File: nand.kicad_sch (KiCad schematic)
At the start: 4 parts, among them Q557 DMP3099L, Q558 2N7002, Q559 2N7002, Q560 DMP3099L

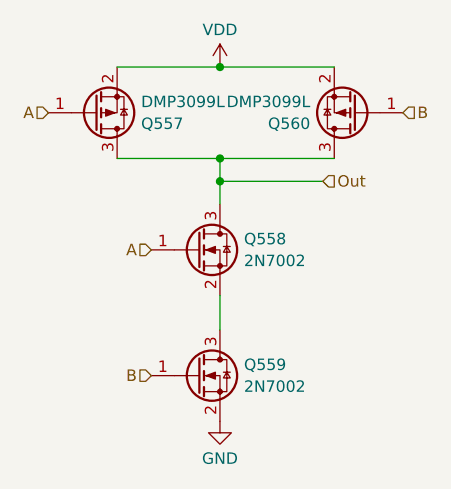
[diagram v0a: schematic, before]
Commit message: added decoupling caps
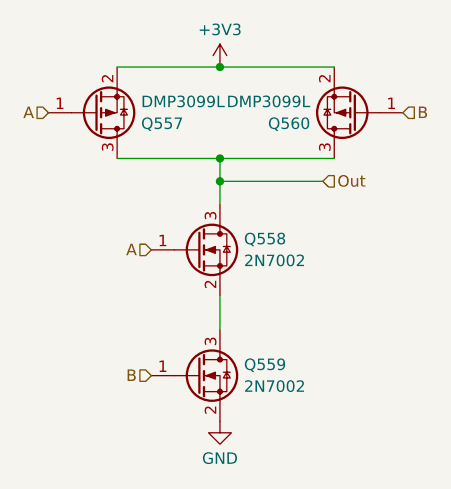
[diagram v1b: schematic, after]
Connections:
- net VDD renamed +3V3
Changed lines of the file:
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@@
+	(wire
+		(pts
+			(xy 115.57 74.93) (xy 128.27 74.93)
+		)
+		(stroke
+			(width 0)
+			(type default)
+		)
+	)
 	(wire
 		(pts
@@
 		(pts
 			(xy 104.14 85.09) (xy 115.57 85.09)
-		)
-		(stroke
-			(width 0)
-			(type default)
-		)
-	)
-	(wire
-		(pts
-			(xy 115.57 74.93) (xy 128.27 74.93)
 		)
 		(stroke
@@
 	)
 	(symbol
-		(lib_id "power:VDD")
+		(lib_id "power:+3V3")
 		(at 115.57 74.93 0)
 		(unit 1)
@@
 			)
 		)
-		(property "Value" "VDD"
+		(property "Value" "+3V3"
 			(at 115.57 70.7969 0)
 			(effects
@@
 			)
 		)
-		(property "Description" "Power symbol creates a global label with name \"VDD\""
+		(property "Description" "Power symbol creates a global label with name \"+3V3\""
 			(at 115.57 74.93 0)
 			(effects

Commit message: corrected output/input type of pins
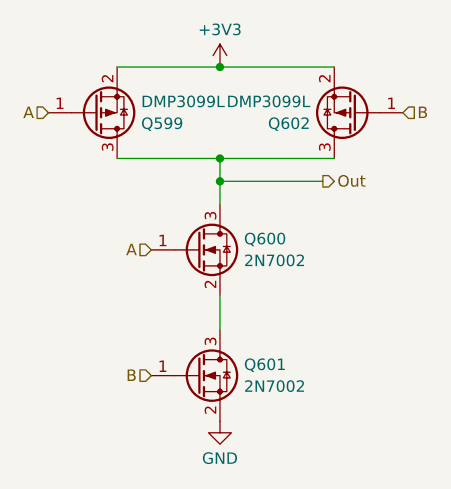
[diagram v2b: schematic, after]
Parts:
- renumbered Q557 to Q599, Q558 to Q600, Q559 to Q601, Q560 to Q602

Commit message: schematic cleanup, routed 1 bdc
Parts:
- renumbered Q599 to Q835, Q600 to Q836, Q601 to Q837, Q602 to Q838

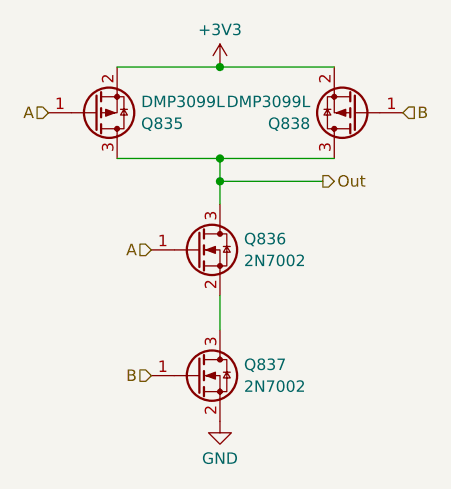
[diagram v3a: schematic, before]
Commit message: started on binary to decimal converter
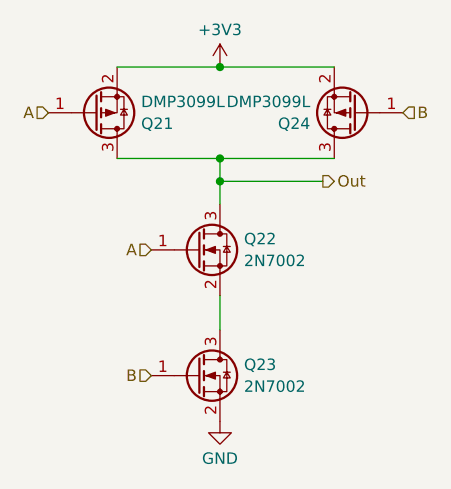
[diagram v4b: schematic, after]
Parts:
- renumbered Q835 to Q21, Q836 to Q22, Q837 to Q23, Q838 to Q24

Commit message: replace bcd logic with bin-to-dec module
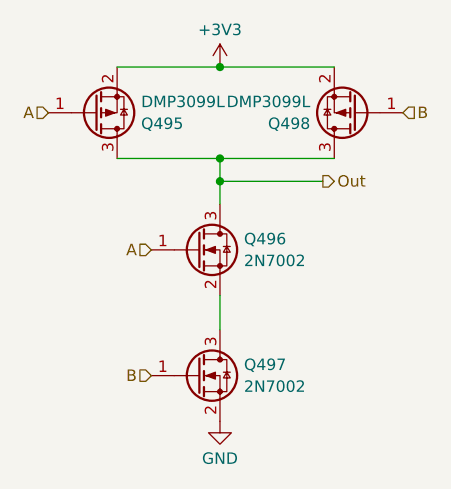
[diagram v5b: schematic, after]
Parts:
- renumbered Q21 to Q495, Q22 to Q496, Q23 to Q497, Q24 to Q498

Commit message: switched to using flipflop module
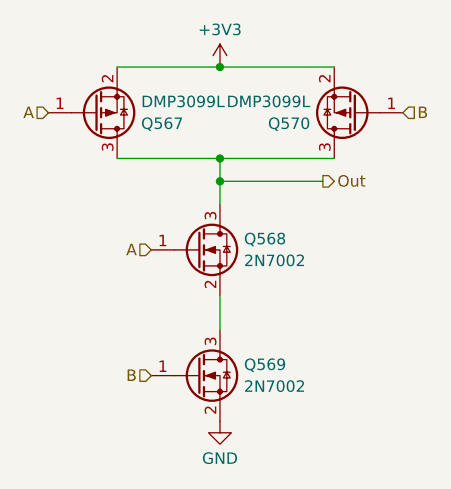
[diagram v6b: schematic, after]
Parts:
- renumbered Q495 to Q567, Q496 to Q568, Q497 to Q569, Q498 to Q570
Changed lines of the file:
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@@
 		(dnp no)
 		(fields_autoplaced yes)
-		(property "Reference" "#PWR0180"
+		(property "Reference" "#PWR0207"
 			(at 115.57 120.65 0)
 			(effects
@@
 		(instances
 			(project "transistor-clock"
-				(path "/ce10d5bc-995e-4952-aa76-0a08f713a0f2/2c36a9e9-de42-4705-9ad4-94f4cc168e2f/213ead95-e2da-4b6f-a756-d929eb6dfb1c/ef45f8fe-f8b4-480d-abd7-c9b5575c64d8"
-					(reference "#PWR0226")
-					(unit 1)
-				)
-				(path "/ce10d5bc-995e-4952-aa76-0a08f713a0f2/2c36a9e9-de42-4705-9ad4-94f4cc168e2f/230aee3b-3cdc-400c-8fed-9199df89dadd/ef45f8fe-f8b4-480d-abd7-c9b5575c64d8"
-					(reference "#PWR0180")
-					(unit 1)
-				)
 				(path "/ce10d5bc-995e-4952-aa76-0a08f713a0f2/2c36a9e9-de42-4705-9ad4-94f4cc168e2f/45f6b4b3-4b31-405d-8488-938c33278b8a/ae3a2682-16ae-4b41-aaac-58f174a956a7"
 					(reference "#PWR0229")
@@
 				(path "/ce10d5bc-995e-4952-aa76-0a08f713a0f2/2c36a9e9-de42-4705-9ad4-94f4cc168e2f/6e22859f-9bca-4d3f-9901-b092abdf20a9/ae3a2682-16ae-4b41-aaac-58f174a956a7"
 					(reference "#PWR0207")
-					(unit 1)
-				)
-				(path "/ce10d5bc-995e-4952-aa76-0a08f713a0f2/2c36a9e9-de42-4705-9ad4-94f4cc168e2f/6fa12e35-b957-4335-be8e-d0857c2dd0bf/ef45f8fe-f8b4-480d-abd7-c9b5575c64d8"
-					(reference "#PWR0204")
 					(unit 1)
 				)
@@
 		(dnp no)
 		(fields_autoplaced yes)
-		(property "Reference" "#PWR0179"
+		(property "Reference" "#PWR0206"
 			(at 115.57 78.74 0)
 			(effects
@@
 		(instances
 			(project "transistor-clock"
-				(path "/ce10d5bc-995e-4952-aa76-0a08f713a0f2/2c36a9e9-de42-4705-9ad4-94f4cc168e2f/213ead95-e2da-4b6f-a756-d929eb6dfb1c/ef45f8fe-f8b4-480d-abd7-c9b5575c64d8"
-					(reference "#PWR0225")
-					(unit 1)
-				)
-				(path "/ce10d5bc-995e-4952-aa76-0a08f713a0f2/2c36a9e9-de42-4705-9ad4-94f4cc168e2f/230aee3b-3cdc-400c-8fed-9199df89dadd/ef45f8fe-f8b4-480d-abd7-c9b5575c64d8"
-					(reference "#PWR0179")
-					(unit 1)
-				)
 				(path "/ce10d5bc-995e-4952-aa76-0a08f713a0f2/2c36a9e9-de42-4705-9ad4-94f4cc168e2f/45f6b4b3-4b31-405d-8488-938c33278b8a/ae3a2682-16ae-4b41-aaac-58f174a956a7"
 					(reference "#PWR0228")
@@
 				(path "/ce10d5bc-995e-4952-aa76-0a08f713a0f2/2c36a9e9-de42-4705-9ad4-94f4cc168e2f/6e22859f-9bca-4d3f-9901-b092abdf20a9/ae3a2682-16ae-4b41-aaac-58f174a956a7"
 					(reference "#PWR0206")
-					(unit 1)
-				)
-				(path "/ce10d5bc-995e-4952-aa76-0a08f713a0f2/2c36a9e9-de42-4705-9ad4-94f4cc168e2f/6fa12e35-b957-4335-be8e-d0857c2dd0bf/ef45f8fe-f8b4-480d-abd7-c9b5575c64d8"
-					(reference "#PWR0203")
 					(unit 1)
 				)
@@
 		(dnp no)
 		(fields_autoplaced yes)
-		(property "Reference" "Q497"
+		(property "Reference" "Q569"
 			(at 118.237 108.0078 0)
 			(effects
@@
 		(instances
 			(project "transistor-clock"
-				(path "/ce10d5bc-995e-4952-aa76-0a08f713a0f2/2c36a9e9-de42-4705-9ad4-94f4cc168e2f/213ead95-e2da-4b6f-a756-d929eb6dfb1c/ef45f8fe-f8b4-480d-abd7-c9b5575c64d8"
-					(reference "Q587")
-					(unit 1)
-				)
-				(path "/ce10d5bc-995e-4952-aa76-0a08f713a0f2/2c36a9e9-de42-4705-9ad4-94f4cc168e2f/230aee3b-3cdc-400c-8fed-9199df89dadd/ef45f8fe-f8b4-480d-abd7-c9b5575c64d8"
-					(reference "Q497")
-					(unit 1)
-				)
 				(path "/ce10d5bc-995e-4952-aa76-0a08f713a0f2/2c36a9e9-de42-4705-9ad4-94f4cc168e2f/45f6b4b3-4b31-405d-8488-938c33278b8a/ae3a2682-16ae-4b41-aaac-58f174a956a7"
 					(reference "Q591")
@@
 				(path "/ce10d5bc-995e-4952-aa76-0a08f713a0f2/2c36a9e9-de42-4705-9ad4-94f4cc168e2f/6e22859f-9bca-4d3f-9901-b092abdf20a9/ae3a2682-16ae-4b41-aaac-58f174a956a7"
 					(reference "Q569")
-					(unit 1)
-				)
-				(path "/ce10d5bc-995e-4952-aa76-0a08f713a0f2/2c36a9e9-de42-4705-9ad4-94f4cc168e2f/6fa12e35-b957-4335-be8e-d0857c2dd0bf/ef45f8fe-f8b4-480d-abd7-c9b5575c64d8"
-					(reference "Q565")
 					(unit 1)
 				)
@@
 		(on_board yes)
 		(dnp no)
-		(property "Reference" "Q498"
+		(property "Reference" "Q570"
 			(at 125.603 81.2222 0)
 			(effects
@@
 		(instances
 			(project "transistor-clock"
-				(path "/ce10d5bc-995e-4952-aa76-0a08f713a0f2/2c36a9e9-de42-4705-9ad4-94f4cc168e2f/213ead95-e2da-4b6f-a756-d929eb6dfb1c/ef45f8fe-f8b4-480d-abd7-c9b5575c64d8"
-					(reference "Q588")
-					(unit 1)
-				)
-				(path "/ce10d5bc-995e-4952-aa76-0a08f713a0f2/2c36a9e9-de42-4705-9ad4-94f4cc168e2f/230aee3b-3cdc-400c-8fed-9199df89dadd/ef45f8fe-f8b4-480d-abd7-c9b5575c64d8"
-					(reference "Q498")
-					(unit 1)
-				)
 				(path "/ce10d5bc-995e-4952-aa76-0a08f713a0f2/2c36a9e9-de42-4705-9ad4-94f4cc168e2f/45f6b4b3-4b31-405d-8488-938c33278b8a/ae3a2682-16ae-4b41-aaac-58f174a956a7"
 					(reference "Q592")
@@
 				(path "/ce10d5bc-995e-4952-aa76-0a08f713a0f2/2c36a9e9-de42-4705-9ad4-94f4cc168e2f/6e22859f-9bca-4d3f-9901-b092abdf20a9/ae3a2682-16ae-4b41-aaac-58f174a956a7"
 					(reference "Q570")
-					(unit 1)
-				)
-				(path "/ce10d5bc-995e-4952-aa76-0a08f713a0f2/2c36a9e9-de42-4705-9ad4-94f4cc168e2f/6fa12e35-b957-4335-be8e-d0857c2dd0bf/ef45f8fe-f8b4-480d-abd7-c9b5575c64d8"
-					(reference "Q566")
 					(unit 1)
 				)
@@
 		(dnp no)
 		(fields_autoplaced yes)
-		(property "Reference" "Q496"
+		(property "Reference" "Q568"
 			(at 118.237 94.0378 0)
 			(effects
@@
 		(instances
 			(project "transistor-clock"
-				(path "/ce10d5bc-995e-4952-aa76-0a08f713a0f2/2c36a9e9-de42-4705-9ad4-94f4cc168e2f/213ead95-e2da-4b6f-a756-d929eb6dfb1c/ef45f8fe-f8b4-480d-abd7-c9b5575c64d8"
-					(reference "Q586")
-					(unit 1)
-				)
-				(path "/ce10d5bc-995e-4952-aa76-0a08f713a0f2/2c36a9e9-de42-4705-9ad4-94f4cc168e2f/230aee3b-3cdc-400c-8fed-9199df89dadd/ef45f8fe-f8b4-480d-abd7-c9b5575c64d8"
-					(reference "Q496")
-					(unit 1)
-				)
 				(path "/ce10d5bc-995e-4952-aa76-0a08f713a0f2/2c36a9e9-de42-4705-9ad4-94f4cc168e2f/45f6b4b3-4b31-405d-8488-938c33278b8a/ae3a2682-16ae-4b41-aaac-58f174a956a7"
 					(reference "Q590")
@@
 				(path "/ce10d5bc-995e-4952-aa76-0a08f713a0f2/2c36a9e9-de42-4705-9ad4-94f4cc168e2f/6e22859f-9bca-4d3f-9901-b092abdf20a9/ae3a2682-16ae-4b41-aaac-58f174a956a7"
 					(reference "Q568")
-					(unit 1)
-				)
-				(path "/ce10d5bc-995e-4952-aa76-0a08f713a0f2/2c36a9e9-de42-4705-9ad4-94f4cc168e2f/6fa12e35-b957-4335-be8e-d0857c2dd0bf/ef45f8fe-f8b4-480d-abd7-c9b5575c64d8"
-					(reference "Q564")
 					(unit 1)
 				)
@@
 		(on_board yes)
 		(dnp no)
-		(property "Reference" "Q495"
+		(property "Reference" "Q567"
 			(at 106.807 81.2222 0)
 			(effects
@@
 		(instances
 			(project "transistor-clock"
-				(path "/ce10d5bc-995e-4952-aa76-0a08f713a0f2/2c36a9e9-de42-4705-9ad4-94f4cc168e2f/213ead95-e2da-4b6f-a756-d929eb6dfb1c/ef45f8fe-f8b4-480d-abd7-c9b5575c64d8"
-					(reference "Q585")
-					(unit 1)
-				)
-				(path "/ce10d5bc-995e-4952-aa76-0a08f713a0f2/2c36a9e9-de42-4705-9ad4-94f4cc168e2f/230aee3b-3cdc-400c-8fed-9199df89dadd/ef45f8fe-f8b4-480d-abd7-c9b5575c64d8"
-					(reference "Q495")
-					(unit 1)
-				)
 				(path "/ce10d5bc-995e-4952-aa76-0a08f713a0f2/2c36a9e9-de42-4705-9ad4-94f4cc168e2f/45f6b4b3-4b31-405d-8488-938c33278b8a/ae3a2682-16ae-4b41-aaac-58f174a956a7"
 					(reference "Q589")
@@
 					(unit 1)
 				)
-				(path "/ce10d5bc-995e-4952-aa76-0a08f713a0f2/2c36a9e9-de42-4705-9ad4-94f4cc168e2f/6fa12e35-b957-4335-be8e-d0857c2dd0bf/ef45f8fe-f8b4-480d-abd7-c9b5575c64d8"
-					(reference "Q563")
-					(unit 1)
-				)
